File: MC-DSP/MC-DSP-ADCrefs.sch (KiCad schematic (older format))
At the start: 33 parts

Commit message: All parts labeled, just need to pick passives basically.
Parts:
- removed U?: REF5030IDGK, Package_SO:MSOP-8_3x3mm_P0.65mm, symbol Reference_Voltage:REF5030IDGK
- added U65: MAX6126AASA, Package_SO:SOIC-8_3.9x4.9mm_P1.27mm, symbol DSP_symbols:MAX6126AASA
- C60, C61, C62, C63, C64, C65, C66, C67, C68, C69, C70, C71, C73, C74: renamed from C?; footprint (none) -> Capacitor_SMD:C_0201_0603Metric_Pad0.64x0.40mm_HandSolder
- C72: renamed from C?; value 0.1uF -> 10uF; footprint (none) -> Capacitor_SMD:C_0201_0603Metric_Pad0.64x0.40mm_HandSolder
- R60, R61, R62, R63, R64, R65, R66, R67, R68, R69, R70, R71: renamed from R?; footprint (none) -> Resistor_SMD:R_0603_1608Metric_Pad0.98x0.95mm_HandSolder
- gave numbers to parts that had none: 5
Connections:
- wire segments 91 -> 106
- no-connect marks 0 -> 2
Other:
- note added: "place near opamps"
- note removed: "FEEDBACK TO MINUS!\n"
- moved on the sheet: C60, C61, C62, C63, C64, C65, C66, C67, C68, C69, C71, C72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

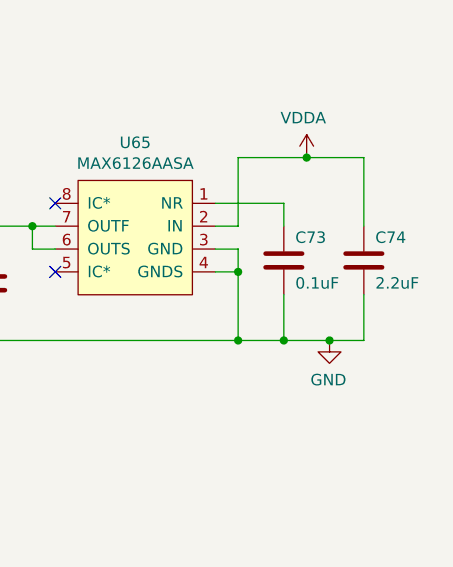
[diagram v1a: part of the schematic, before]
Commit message: DSP - added footprints and links to most parts
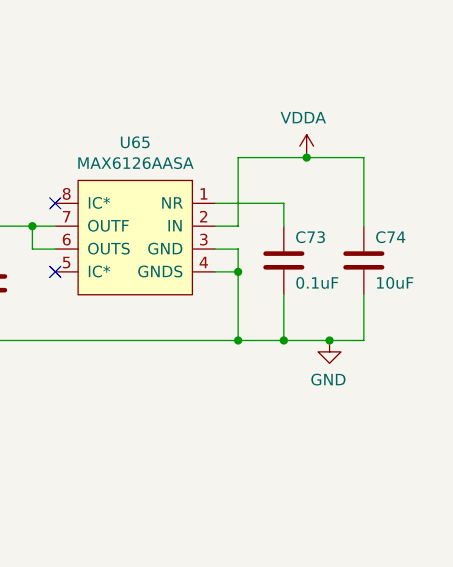
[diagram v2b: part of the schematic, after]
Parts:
- C74: value 2.2uF -> 10uF

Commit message: Removed clock buffer, misc leds, ethernet
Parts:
- C60, C61, C62, C63, C64, C65, C66, C67, C68, C69, C70, C71, C72, C73, C74: footprint Capacitor_SMD:C_0201_0603Metric_Pad0.64x0.40mm_HandSolder -> Capacitor_SMD:C_0603_1608Metric_Pad1.08x0.95mm_HandSolder
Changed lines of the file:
@@
 $Descr A4 11693 8268
 encoding utf-8
-Sheet 9 9
+Sheet 9 7
 Title ""
 Date ""
@@
 F 0 "C69" H 4000 5800 50  0000 R CNN
 F 1 "22uF" H 4000 6000 50  0000 R CNN
-F 2 "Capacitor_SMD:C_0201_0603Metric_Pad0.64x0.40mm_HandSolder" H 4088 5750 50  0001 C CNN
+F 2 "Capacitor_SMD:C_0603_1608Metric_Pad1.08x0.95mm_HandSolder" H 4088 5750 50  0001 C CNN
 F 3 "https://www.digikey.com/en/products/detail/walsin-technology-corporation/0603B103K500CT/9354883" H 4050 5900 50  0001 C CNN
 	1    4050 5900
@@
 F 0 "C68" H 3700 5800 50  0000 R CNN
 F 1 "22uF" H 3700 6000 50  0000 R CNN
-F 2 "Capacitor_SMD:C_0201_0603Metric_Pad0.64x0.40mm_HandSolder" H 3788 5750 50  0001 C CNN
+F 2 "Capacitor_SMD:C_0603_1608Metric_Pad1.08x0.95mm_HandSolder" H 3788 5750 50  0001 C CNN
 F 3 "https://www.digikey.com/en/products/detail/walsin-technology-corporation/0603B103K500CT/9354883" H 3750 5900 50  0001 C CNN
 	1    3750 5900
@@
 F 0 "C67" H 3400 5800 50  0000 R CNN
 F 1 "22uF" H 3400 6000 50  0000 R CNN
-F 2 "Capacitor_SMD:C_0201_0603Metric_Pad0.64x0.40mm_HandSolder" H 3488 5750 50  0001 C CNN
+F 2 "Capacitor_SMD:C_0603_1608Metric_Pad1.08x0.95mm_HandSolder" H 3488 5750 50  0001 C CNN
 F 3 "https://www.digikey.com/en/products/detail/walsin-technology-corporation/0603B103K500CT/9354883" H 3450 5900 50  0001 C CNN
 	1    3450 5900
@@
 F 0 "C66" H 3100 5800 50  0000 R CNN
 F 1 "22uF" H 3100 6000 50  0000 R CNN
-F 2 "Capacitor_SMD:C_0201_0603Metric_Pad0.64x0.40mm_HandSolder" H 3188 5750 50  0001 C CNN
+F 2 "Capacitor_SMD:C_0603_1608Metric_Pad1.08x0.95mm_HandSolder" H 3188 5750 50  0001 C CNN
 F 3 "https://www.digikey.com/en/products/detail/walsin-technology-corporation/0603B103K500CT/9354883" H 3150 5900 50  0001 C CNN
 	1    3150 5900
@@
 F 0 "C60" H 6850 1350 50  0000 R CNN
 F 1 "0.1uF" H 6850 1550 50  0000 R CNN
-F 2 "Capacitor_SMD:C_0201_0603Metric_Pad0.64x0.40mm_HandSolder" H 6938 1300 50  0001 C CNN
+F 2 "Capacitor_SMD:C_0603_1608Metric_Pad1.08x0.95mm_HandSolder" H 6938 1300 50  0001 C CNN
 F 3 "https://www.digikey.com/en/products/detail/yageo/CC0603KRX7R9BB104/2103082" H 6900 1450 50  0001 C CNN
 	1    6900 1450
@@
 F 0 "C74" H 9950 4750 50  0000 R CNN
 F 1 "10uF" H 9950 4950 50  0000 R CNN
-F 2 "Capacitor_SMD:C_0201_0603Metric_Pad0.64x0.40mm_HandSolder" H 10038 4700 50  0001 C CNN
+F 2 "Capacitor_SMD:C_0603_1608Metric_Pad1.08x0.95mm_HandSolder" H 10038 4700 50  0001 C CNN
 F 3 "https://www.digikey.com/en/products/detail/kemet/C0603C104K5RECAUTO/6575893?s=N4IgjCBcpgLFoDGUBmBDANgZwKYBoQB7KAbRACYBmADgHYaQBdAgBwBcoQBlNgJwEsAdgHMQAXwJgAbAhDJI6bPiKkQlAJzlYM5iHaceAkeIIBacrPl8ArsuKQyAVhAF1TCSFNvocqDbuqEIxiHhYO4AAM1gBiTAQyPvwAJpymYBEWrByQIC4gbACeLDicSVjIIUA" H 10000 4850 50  0001 C CNN
 	1    10000 4850
@@
 F 0 "C73" H 9600 4750 50  0000 R CNN
 F 1 "0.1uF" H 9600 4950 50  0000 R CNN
-F 2 "Capacitor_SMD:C_0201_0603Metric_Pad0.64x0.40mm_HandSolder" H 9688 4700 50  0001 C CNN
+F 2 "Capacitor_SMD:C_0603_1608Metric_Pad1.08x0.95mm_HandSolder" H 9688 4700 50  0001 C CNN
 F 3 "https://www.digikey.com/en/products/detail/yageo/CC0603KRX7R9BB104/2103082" H 9650 4850 50  0001 C CNN
 	1    9650 4850
@@
 F 0 "C72" H 8300 4850 50  0000 R CNN
 F 1 "10uF" H 8300 5050 50  0000 R CNN
-F 2 "Capacitor_SMD:C_0201_0603Metric_Pad0.64x0.40mm_HandSolder" H 8388 4800 50  0001 C CNN
+F 2 "Capacitor_SMD:C_0603_1608Metric_Pad1.08x0.95mm_HandSolder" H 8388 4800 50  0001 C CNN
 F 3 "https://www.digikey.com/en/products/detail/kemet/C0603C104K5RECAUTO/6575893?s=N4IgjCBcpgLFoDGUBmBDANgZwKYBoQB7KAbRACYBmADgHYaQBdAgBwBcoQBlNgJwEsAdgHMQAXwJgAbAhDJI6bPiKkQlAJzlYM5iHaceAkeIIBacrPl8ArsuKQyAVhAF1TCSFNvocqDbuqEIxiHhYO4AAM1gBiTAQyPvwAJpymYBEWrByQIC4gbACeLDicSVjIIUA" H 8350 4950 50  0001 C CNN
 	1    8350 4950
@@
 F 0 "C71" H 7050 4850 50  0000 R CNN
 F 1 "0.1uF" H 7050 5050 50  0000 R CNN
-F 2 "Capacitor_SMD:C_0201_0603Metric_Pad0.64x0.40mm_HandSolder" H 7138 4800 50  0001 C CNN
+F 2 "Capacitor_SMD:C_0603_1608Metric_Pad1.08x0.95mm_HandSolder" H 7138 4800 50  0001 C CNN
 F 3 "https://www.digikey.com/en/products/detail/yageo/CC0603KRX7R9BB104/2103082" H 7100 4950 50  0001 C CNN
 	1    7100 4950
@@
 F 0 "C70" H 6450 4850 50  0000 R CNN
 F 1 "0.1uF" H 6450 5050 50  0000 R CNN
-F 2 "Capacitor_SMD:C_0201_0603Metric_Pad0.64x0.40mm_HandSolder" H 6538 4800 50  0001 C CNN
+F 2 "Capacitor_SMD:C_0603_1608Metric_Pad1.08x0.95mm_HandSolder" H 6538 4800 50  0001 C CNN
 F 3 "https://www.digikey.com/en/products/detail/yageo/CC0603KRX7R9BB104/2103082" H 6500 4950 50  0001 C CNN
 	1    6500 4950
@@
 F 0 "C61" H 7150 1350 50  0000 R CNN
 F 1 "0.1uF" H 7150 1550 50  0000 R CNN
-F 2 "Capacitor_SMD:C_0201_0603Metric_Pad0.64x0.40mm_HandSolder" H 7238 1300 50  0001 C CNN
+F 2 "Capacitor_SMD:C_0603_1608Metric_Pad1.08x0.95mm_HandSolder" H 7238 1300 50  0001 C CNN
 F 3 "https://www.digikey.com/en/products/detail/yageo/CC0603KRX7R9BB104/2103082" H 7200 1450 50  0001 C CNN
 	1    7200 1450
@@
 F 0 "C62" H 7450 1350 50  0000 R CNN
 F 1 "0.1uF" H 7450 1550 50  0000 R CNN
-F 2 "Capacitor_SMD:C_0201_0603Metric_Pad0.64x0.40mm_HandSolder" H 7538 1300 50  0001 C CNN
+F 2 "Capacitor_SMD:C_0603_1608Metric_Pad1.08x0.95mm_HandSolder" H 7538 1300 50  0001 C CNN
 F 3 "https://www.digikey.com/en/products/detail/yageo/CC0603KRX7R9BB104/2103082" H 7500 1450 50  0001 C CNN
 	1    7500 1450
@@
 F 0 "C63" H 7750 1350 50  0000 R CNN
 F 1 "0.1uF" H 7750 1550 50  0000 R CNN
-F 2 "Capacitor_SMD:C_0201_0603Metric_Pad0.64x0.40mm_HandSolder" H 7838 1300 50  0001 C CNN
+F 2 "Capacitor_SMD:C_0603_1608Metric_Pad1.08x0.95mm_HandSolder" H 7838 1300 50  0001 C CNN
 F 3 "https://www.digikey.com/en/products/detail/yageo/CC0603KRX7R9BB104/2103082" H 7800 1450 50  0001 C CNN
 	1    7800 1450
@@
 F 0 "C64" H 8050 1350 50  0000 R CNN
 F 1 "0.1uF" H 8050 1550 50  0000 R CNN
-F 2 "Capacitor_SMD:C_0201_0603Metric_Pad0.64x0.40mm_HandSolder" H 8138 1300 50  0001 C CNN
+F 2 "Capacitor_SMD:C_0603_1608Metric_Pad1.08x0.95mm_HandSolder" H 8138 1300 50  0001 C CNN
 F 3 "https://www.digikey.com/en/products/detail/yageo/CC0603KRX7R9BB104/2103082" H 8100 1450 50  0001 C CNN
 	1    8100 1450
@@
 F 0 "C65" H 2800 5800 50  0000 R CNN
 F 1 "22uF" H 2800 6000 50  0000 R CNN
-F 2 "Capacitor_SMD:C_0201_0603Metric_Pad0.64x0.40mm_HandSolder" H 2888 5750 50  0001 C CNN
+F 2 "Capacitor_SMD:C_0603_1608Metric_Pad1.08x0.95mm_HandSolder" H 2888 5750 50  0001 C CNN
 F 3 "https://www.digikey.com/en/products/detail/walsin-technology-corporation/0603B103K500CT/9354883" H 2850 5900 50  0001 C CNN
 	1    2850 5900

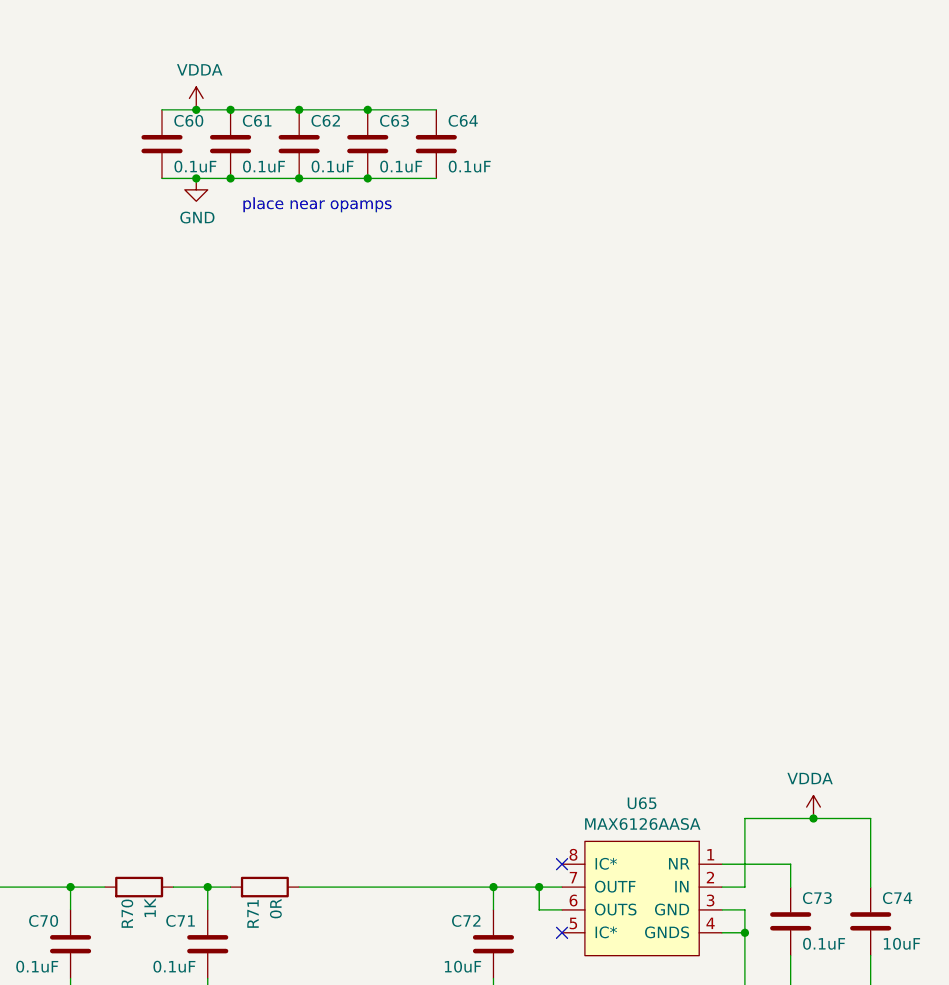
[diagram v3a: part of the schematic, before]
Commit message: Total overhaul of power planes. Routed whole Analog section, middle of digital section.
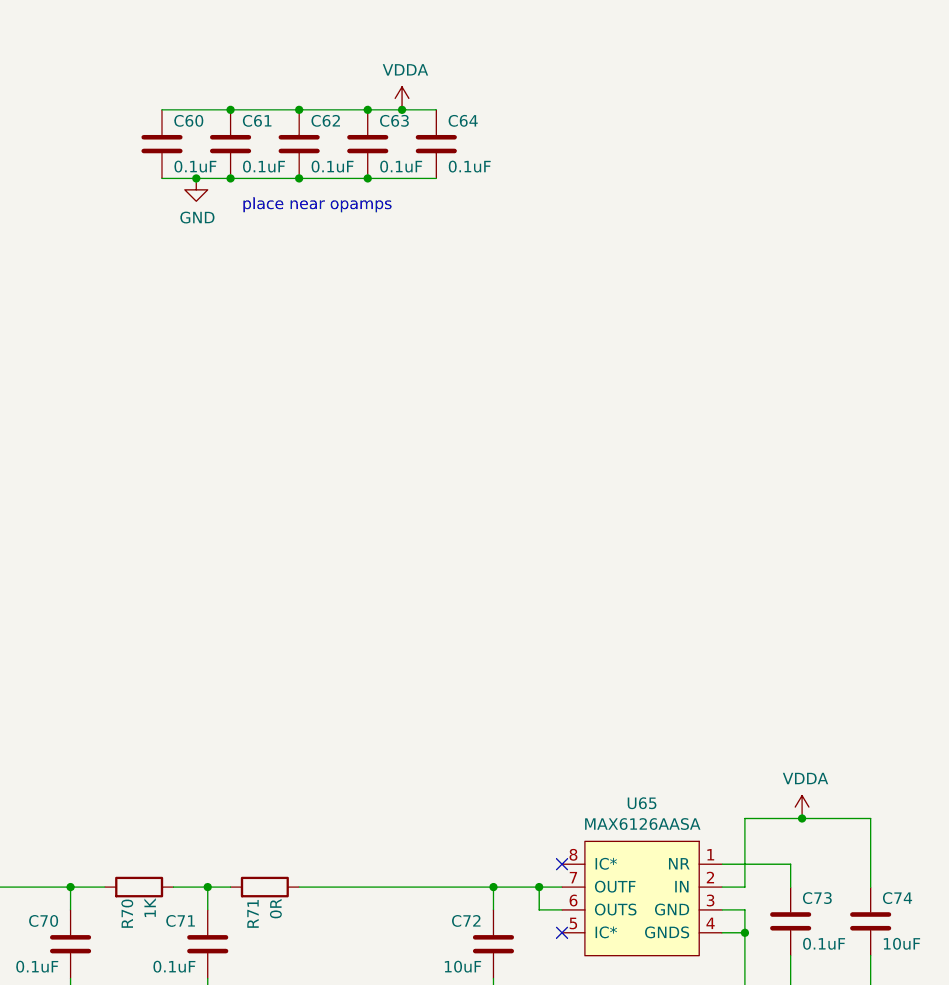
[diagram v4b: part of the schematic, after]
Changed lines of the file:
@@
 $Descr A4 11693 8268
 encoding utf-8
-Sheet 9 7
+Sheet 4 7
 Title ""
 Date ""
@@
 	1    6900 1450
 	-1   0    0    1
-$EndComp
-$Comp
-L power:VDDA #PWR0188
-U 1 1 621E7DC6
-P 7050 1300
-F 0 "#PWR0188" H 7050 1150 50  0001 C CNN
-F 1 "VDDA" H 7065 1473 50  0000 C CNN
-F 2 "" H 7050 1300 50  0001 C CNN
-F 3 "" H 7050 1300 50  0001 C CNN
-	1    7050 1300
-	1    0    0    -1
 $EndComp
 $Comp
@@
 $EndComp
 $Comp
-L power:VDDA #PWR0191
-U 1 1 623334D4
-P 5450 1000
-F 0 "#PWR0191" H 5450 850 50  0001 C CNN
-F 1 "VDDA" H 5300 1050 50  0000 C CNN
-F 2 "" H 5450 1000 50  0001 C CNN
-F 3 "" H 5450 1000 50  0001 C CNN
-	1    5450 1000
-	1    0    0    -1
-$EndComp
-$Comp
 L Device:C C61
 U 1 1 6233EFBA
@@
 	-1   0    0    1
 $EndComp
-Wire Wire Line
-	7050 1300 6900 1300
 Connection ~ 7200 1300
 Wire Wire Line
@@
 Connection ~ 7800 1300
 Wire Wire Line
-	7800 1300 8100 1300
-Wire Wire Line
 	6900 1600 7050 1600
 Connection ~ 7200 1600
@@
 Wire Wire Line
 	7800 1600 8100 1600
-Connection ~ 7050 1300
-Wire Wire Line
-	7050 1300 7200 1300
 Connection ~ 7050 1600
 Wire Wire Line
@@
 F 3 "" H 5450 2500 50  0001 C CNN
 	1    5450 2500
-	1    0    0    -1
-$EndComp
-$Comp
-L power:VDDA #PWR0193
-U 1 1 6235C17A
-P 5450 1900
-F 0 "#PWR0193" H 5450 1750 50  0001 C CNN
-F 1 "VDDA" H 5300 1950 50  0000 C CNN
-F 2 "" H 5450 1900 50  0001 C CNN
-F 3 "" H 5450 1900 50  0001 C CNN
-	1    5450 1900
 	1    0    0    -1
 $EndComp
@@
 $EndComp
 $Comp
-L power:VDDA #PWR0195
-U 1 1 62361DC1
-P 5450 2800
-F 0 "#PWR0195" H 5450 2650 50  0001 C CNN
-F 1 "VDDA" H 5300 2850 50  0000 C CNN
-F 2 "" H 5450 2800 50  0001 C CNN
-F 3 "" H 5450 2800 50  0001 C CNN
-	1    5450 2800
-	1    0    0    -1
-$EndComp
-$Comp
 L Device:R R63
 U 1 1 623678B7
@@
 $EndComp
 $Comp
-L power:VDDA #PWR0197
-U 1 1 623678E0
-P 5450 3700
-F 0 "#PWR0197" H 5450 3550 50  0001 C CNN
-F 1 "VDDA" H 5300 3750 50  0000 C CNN
-F 2 "" H 5450 3700 50  0001 C CNN
-F 3 "" H 5450 3700 50  0001 C CNN
-	1    5450 3700
-	1    0    0    -1
-$EndComp
-$Comp
 L Device:R R64
 U 1 1 62383A84
@@
 $EndComp
 $Comp
-L power:VDDA #PWR0199
-U 1 1 62383AAD
-P 5450 4600
-F 0 "#PWR0199" H 5450 4450 50  0001 C CNN
-F 1 "VDDA" H 5300 4650 50  0000 C CNN
-F 2 "" H 5450 4600 50  0001 C CNN
-F 3 "" H 5450 4600 50  0001 C CNN
-	1    5450 4600
-	1    0    0    -1
-$EndComp
-$Comp
 L Device:R R65
 U 1 1 623B32D5
@@
 Wire Wire Line
 	2850 1300 2850 5350
-$Comp
-L power:VDDA #PWR0200
-U 1 1 621E8B2D
-P 9750 4400
-F 0 "#PWR0200" H 9750 4250 50  0001 C CNN
-F 1 "VDDA" H 9765 4573 50  0000 C CNN
-F 2 "" H 9750 4400 50  0001 C CNN
-F 3 "" H 9750 4400 50  0001 C CNN
-	1    9750 4400
-	-1   0    0    -1
-$EndComp
 Wire Wire Line
 	4850 1300 4900 1300
@@
 	9650 5200 9850 5200
 Wire Wire Line
-	9750 4400 9450 4400
-Wire Wire Line
 	9350 4600 9650 4600
 Wire Wire Line
@@
 Wire Wire Line
 	10000 5200 9850 5200
-Connection ~ 9750 4400
-Wire Wire Line
-	9750 4400 10000 4400
 Connection ~ 9850 5200
+Wire Wire Line
+	6900 1300 7200 1300
+$Comp
+L power:VDDA #PWR?
+U 1 1 6317CDF1
+P 9700 4400
+AR Path="/6317CDF1" Ref="#PWR?"  Part="1"
+AR Path="/62086B6E/6317CDF1" Ref="#PWR0143"  Part="1"
+F 0 "#PWR0143" H 9700 4250 50  0001 C CNN
+F 1 "VDDA" H 9715 4573 50  0000 C CNN
+F 2 "" H 9700 4400 50  0001 C CNN
+F 3 "" H 9700 4400 50  0001 C CNN
+	1    9700 4400
+	1    0    0    -1
+$EndComp
+Wire Wire Line
+	9450 4400 9700 4400
+Connection ~ 9700 4400
+Wire Wire Line
+	9700 4400 10000 4400
+$Comp
+L power:VDDA #PWR?
+U 1 1 6317FFAD
+P 5450 1000
+AR Path="/6317FFAD" Ref="#PWR?"  Part="1"
+AR Path="/62086B6E/6317FFAD" Ref="#PWR0144"  Part="1"
+F 0 "#PWR0144" H 5450 850 50  0001 C CNN
+F 1 "VDDA" H 5300 1050 50  0000 C CNN
+F 2 "" H 5450 1000 50  0001 C CNN
+F 3 "" H 5450 1000 50  0001 C CNN
+	1    5450 1000
+	1    0    0    -1
+$EndComp
+Wire Wire Line
+	7800 1300 7950 1300
+$Comp
+L power:VDDA #PWR?
+U 1 1 63180727
+P 7950 1300
+AR Path="/63180727" Ref="#PWR?"  Part="1"
+AR Path="/62086B6E/63180727" Ref="#PWR0145"  Part="1"
+F 0 "#PWR0145" H 7950 1150 50  0001 C CNN
+F 1 "VDDA" H 7965 1473 50  0000 C CNN
+F 2 "" H 7950 1300 50  0001 C CNN
+F 3 "" H 7950 1300 50  0001 C CNN
+	1    7950 1300
+	1    0    0    -1
+$EndComp
+Connection ~ 7950 1300
+Wire Wire Line
+	7950 1300 8100 1300
+$Comp
+L power:VDDA #PWR?
+U 1 1 63180C45
+P 5450 1900
+AR Path="/63180C45" Ref="#PWR?"  Part="1"
+AR Path="/62086B6E/63180C45" Ref="#PWR0146"  Part="1"
+F 0 "#PWR0146" H 5450 1750 50  0001 C CNN
+F 1 "VDDA" H 5300 1950 50  0000 C CNN
+F 2 "" H 5450 1900 50  0001 C CNN
+F 3 "" H 5450 1900 50  0001 C CNN
+	1    5450 1900
+	1    0    0    -1
+$EndComp
+$Comp
+L power:VDDA #PWR?
+U 1 1 63181027
+P 5450 2800
+AR Path="/63181027" Ref="#PWR?"  Part="1"
+AR Path="/62086B6E/63181027" Ref="#PWR0147"  Part="1"
+F 0 "#PWR0147" H 5450 2650 50  0001 C CNN
+F 1 "VDDA" H 5300 2850 50  0000 C CNN
+F 2 "" H 5450 2800 50  0001 C CNN
+F 3 "" H 5450 2800 50  0001 C CNN
+	1    5450 2800
+	1    0    0    -1
+$EndComp
+$Comp
+L power:VDDA #PWR?
+U 1 1 631814CE
+P 5450 3700
+AR Path="/631814CE" Ref="#PWR?"  Part="1"
+AR Path="/62086B6E/631814CE" Ref="#PWR0148"  Part="1"
+F 0 "#PWR0148" H 5450 3550 50  0001 C CNN
+F 1 "VDDA" H 5300 3750 50  0000 C CNN
+F 2 "" H 5450 3700 50  0001 C CNN
+F 3 "" H 5450 3700 50  0001 C CNN
+	1    5450 3700
+	1    0    0    -1
+$EndComp
+$Comp
+L power:VDDA #PWR?
+U 1 1 63181B93
+P 5450 4600
+AR Path="/63181B93" Ref="#PWR?"  Part="1"
+AR Path="/62086B6E/63181B93" Ref="#PWR0149"  Part="1"
+F 0 "#PWR0149" H 5450 4450 50  0001 C CNN
+F 1 "VDDA" H 5300 4650 50  0000 C CNN
+F 2 "" H 5450 4600 50  0001 C CNN
+F 3 "" H 5450 4600 50  0001 C CNN
+	1    5450 4600
+	1    0    0    -1
+$EndComp
 $EndSCHEMATC
